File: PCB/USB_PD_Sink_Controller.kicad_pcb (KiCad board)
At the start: 2 copper layers, 43.5 x 30.8 mm, 26 parts, among them J1 USB_C_Receptacle_PowerOnly_6P, J2 JST_01x02_Socket, U1 STUSB4500QTR, U2 STL6P3LLH6, U3 STL6P3LLH6

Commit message: Added Ground plane and started LDO addition to SCH
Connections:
- A1 pad 27: unconnected-(A1-+5V-Pad27) -> Net-(A1-+5V)
- A1 pad 30: unconnected-(A1-VIN-Pad30) -> /Vbus
- J2 pad 1: Net-(D4-K) -> GND
- J2 pad 2: GND -> Net-(D4-K)
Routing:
- net GND: track 154.9 -> 72.1 mm
- net /Vbus: track 45.2 -> 78.7 mm
- net Net-(D4-K): track 18.9 -> 19.8 mm
- added copper zone on B.Cu, net GND

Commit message: Made the Arduino esp32 and added a diode to prevent reverse voltage
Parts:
- added D5: D, Diode_SMD:D_0603_1608Metric_Pad1.05x0.95mm_HandSolder, F.Cu at (350.5, 124.2)
- A1: value Arduino_Nano_v2.x -> Arduino_Nano_ESP32
- J2: footprint Connector_JST:JST_XH_B2B-XH-AM_1x02_P2.50mm_Vertical -> Connector_JST:JST_XH_B2B-XH-A_1x02_P2.50mm_Vertical
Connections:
- A1 pad 17: unconnected-(A1-3V3-Pad17) -> /VSYS
- A1 pad 27: Net-(A1-+5V) -> unconnected-(A1-VUSB/5V-Pad27)
- A1 pad 30: /Vbus -> Net-(A1-VIN)
- U1 pad 22: GND -> /VSYS
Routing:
- net /VSYS: track 0.00 -> 29.0 mm, vias 0 -> 2
- net GND: track 72.1 -> 44.9 mm, vias 1 -> 3
- net /DISCH: track 0.00 -> 24.7 mm, vias 0 -> 2
- net /Vbus: track 78.7 -> 59.1 mm, vias 4 -> 5
- net Net-(A1-VIN): track 0.00 -> 19.2 mm
- net Net-(U2-G): track 13.6 -> 14.8 mm, vias 0 -> 2
- net Net-(U1-VREG_2V7): track 1.92 -> 2.69 mm

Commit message: Updated PCB
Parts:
- removed A1: Arduino_Nano_ESP32, Module:Arduino_Nano
- removed D5: D, Diode_SMD:D_0603_1608Metric_Pad1.05x0.95mm_HandSolder
- added J3: JST_01x05_Socket, Connector_JST:JST_XH_B5B-XH-A_1x05_P2.50mm_Vertical, F.Cu at (345.5, 122.0)
- moved R7 18.1 mm to (328.9, 124.5)
- moved R6 13.3 mm to (340.5, 120.0)
- moved D4 9.13 mm to (341.5, 124.6), turned to -90 degrees
- moved R9 5.82 mm to (334.3, 122.3), turned to 0 degrees
- moved R8 5.06 mm to (338.7, 125.1)
- moved R10 4.43 mm to (340.5, 121.6), turned to 0 degrees
- moved R5 4.30 mm to (347.0, 118.2)
- moved C6 4.00 mm to (347.0, 116.8)
- moved R3 3.64 mm to (343.5, 118.2)
- moved J2 2.72 mm to (353.0, 115.0), turned to 0 degrees
- moved U2 2.51 mm to (342.4, 114.0)
- moved R4 2.50 mm to (343.5, 116.8), turned to 0 degrees
- moved U3 2.45 mm to (347.5, 114.0)
- moved R1 1.77 mm to (334.0, 118.0)
- moved R2 1.28 mm to (334.5, 119.5)
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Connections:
- C1 pad 1: /Vbus -> /VDD
- C3 pad 1: GND -> /VDD
- C3 pad 2: /VDD -> GND
- C4 pad 1: GND -> Net-(U1-VREG_2V7)
- C4 pad 2: Net-(U1-VREG_2V7) -> GND
- C5 pad 1: GND -> Net-(U1-VREG_1V2)
- C5 pad 2: Net-(U1-VREG_1V2) -> GND
- D1 pad 1: /Vbus -> /VDD
- D3 pad 2: /Vbus -> /VDD
- J1 pad A9: /Vbus -> /VDD
- J1 pad B9: /Vbus -> /VDD
- R1 pad 1: /Vbus -> /VDD
- R10 pad 1: Net-(A1-SDA/A4) -> Net-(U1-SDA)
- R4 pad 2: /VDD -> Net-(U2-S)
- R7 pad 1: /RESET -> GND
- R7 pad 2: GND -> /RESET
- R8 pad 1: Net-(A1-D3) -> /ALERT
- R8 pad 2: /ALERT -> Net-(U1-SCL)
- R9 pad 1: Net-(A1-SCL/A5) -> Net-(U1-ALERT)
- U1 pad 19: /SCL -> Net-(U1-ALERT)
- U1 pad 22: /VSYS -> /3V3
- U1 pad 7: /ALERT -> Net-(U1-SCL)
- U1 pad 8: /SDA -> Net-(U1-SDA)
- U2 pad 2: /VDD -> Net-(U2-S)
- U2 pad 3: /Vbus -> /VDD
- U3 pad 2: /VDD -> Net-(U2-S)
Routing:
- net /Vbus: track 59.1 -> 0.00 mm, vias 5 -> 0
- net /VDD: track 22.7 -> 52.0 mm, vias 2 -> 4
- net /VSYS: track 29.0 -> 0.00 mm, vias 2 -> 0
- net /RESET: track 27.9 -> 2.48 mm, vias 1 -> 0
- net Net-(D4-K): track 19.8 -> 44.7 mm
- net /3V3: track 0.00 -> 22.2 mm, vias 0 -> 1
- net Net-(A1-SCL/A5): track 22.0 -> 0.00 mm, vias 2 -> 0
- net Net-(A1-SDA/A4): track 21.9 -> 0.00 mm, vias 2 -> 0
- net Net-(A1-VIN): track 19.2 -> 0.00 mm
- net Net-(U1-SDA): track 0.00 -> 14.1 mm
- net /DISCH: track 24.7 -> 12.3 mm, vias 2 -> 0
- net Net-(U1-SCL): track 0.00 -> 11.5 mm
- net /SCL: track 9.69 -> 20.6 mm
- net GND: track 44.9 -> 36.2 mm
- net Net-(A1-D3): track 7.64 -> 0.00 mm, vias 2 -> 0
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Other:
- board size 43.5 x 30.8 mm -> 43.5 x 13.9 mm
- board text added: "3V3"
- board text added: "ALT"
- board text added: "GND"
- board text added: "SCL"
- board text added: "SDA"
- board text added: "VBUS"

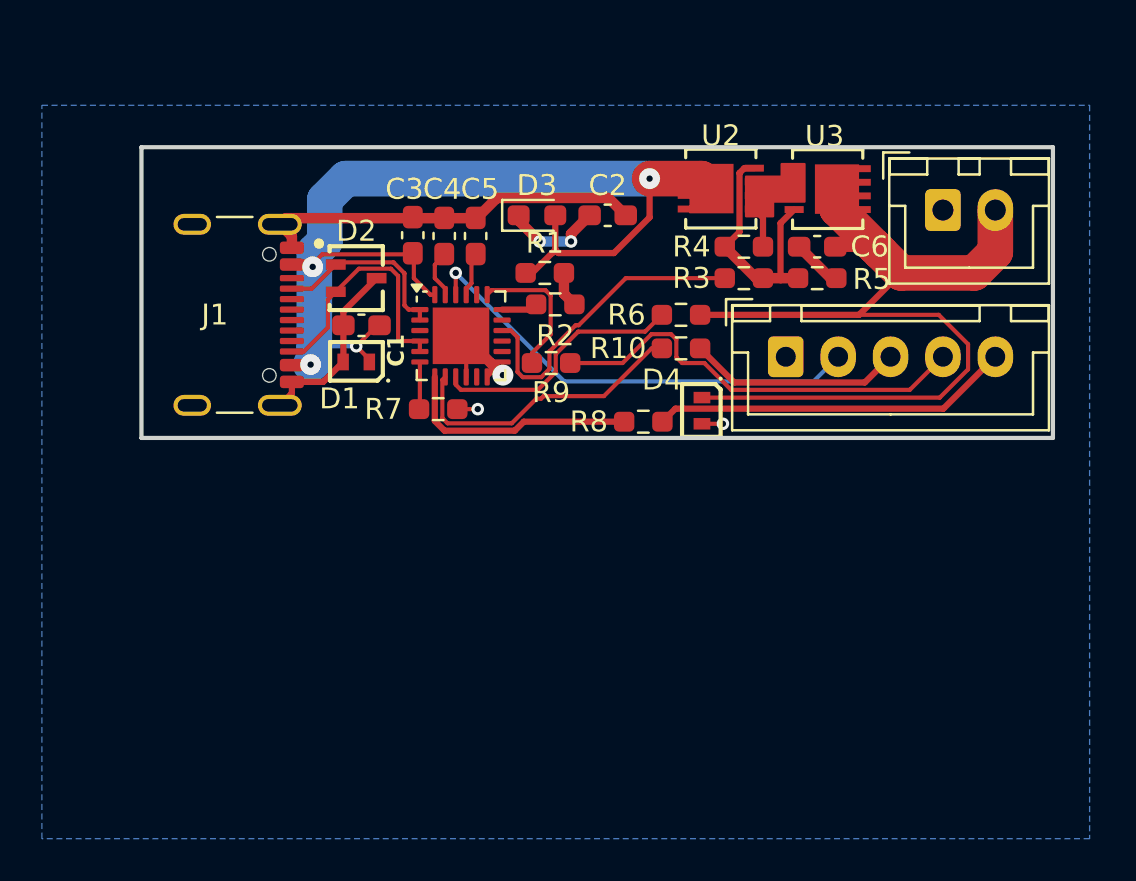
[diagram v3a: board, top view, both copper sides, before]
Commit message: Made min VBUS main and added BOM
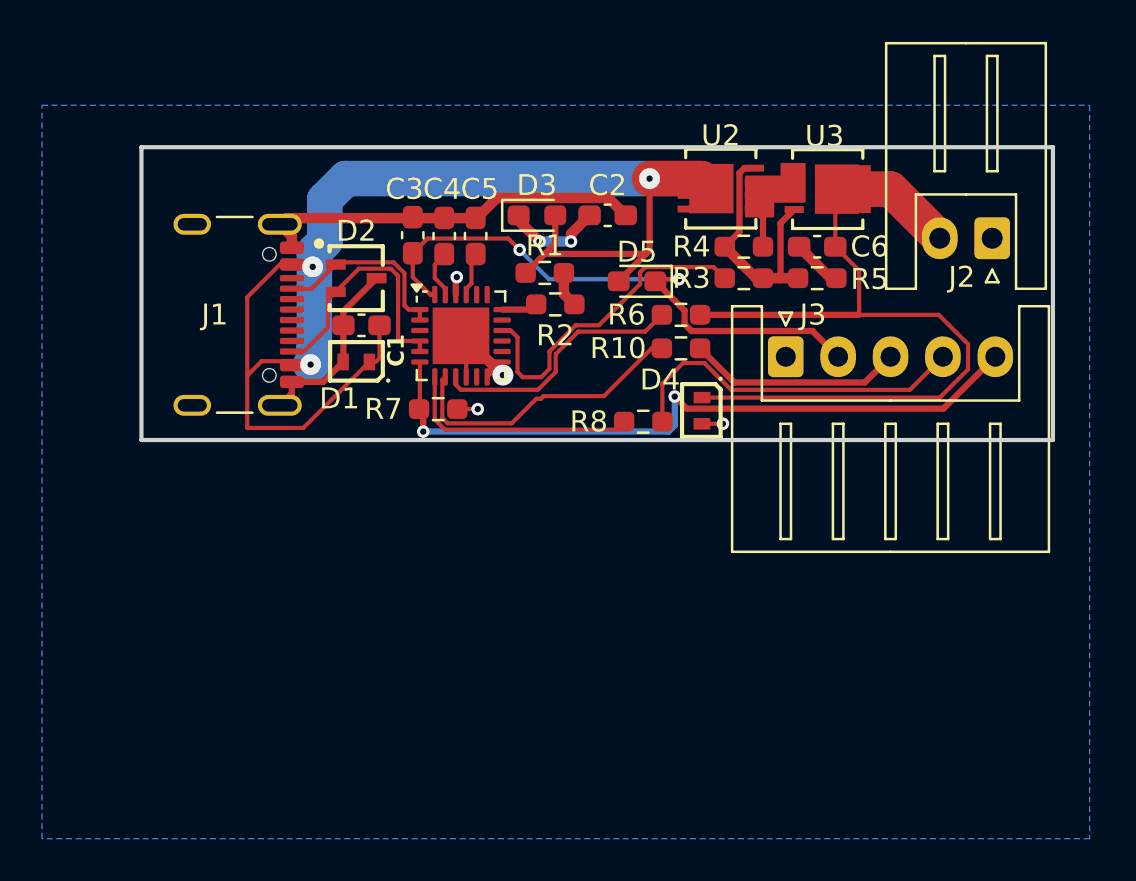
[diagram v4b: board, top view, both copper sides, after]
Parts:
- removed R9: 4.7kR, Resistor_SMD:R_0603_1608Metric_Pad0.98x0.95mm_HandSolder
- added D5: D, Diode_SMD:D_0603_1608Metric_Pad1.05x0.95mm_HandSolder, F.Cu at (338.4, 118.4)
- J2: footprint Connector_JST:JST_XH_B2B-XH-A_1x02_P2.50mm_Vertical -> Connector_JST:JST_XH_S2B-XH-A_1x02_P2.50mm_Horizontal
- J3: footprint Connector_JST:JST_XH_B5B-XH-A_1x05_P2.50mm_Vertical -> Connector_JST:JST_XH_S5B-XH-A_1x05_P2.50mm_Horizontal
- moved J2 2.71 mm to (355.4, 116.3), turned to 180 degrees
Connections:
- C1 pad 1: /VDD -> /Vbus
- D1 pad 1: /VDD -> /Vbus
- D3 pad 2: /VDD -> /Vbus
- J1 pad A9: /VDD -> /Vbus
- J1 pad B9: /VDD -> /Vbus
- J3 pad 2: /3V3 -> /VDD
- J3 pad 5: /ALERT -> /RESET
- R1 pad 1: /VDD -> /Vbus
- R8 pad 1: /ALERT -> /SCL
- U1 pad 19: Net-(U1-ALERT) -> unconnected-(U1-ALERT-Pad19)
- U1 pad 22: /3V3 -> GND
- U2 pad 3: /VDD -> /Vbus
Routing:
- net /Vbus: track 0.00 -> 63.7 mm, vias 0 -> 3
- net /RESET: track 2.48 -> 33.6 mm, vias 0 -> 2
- net /VDD: track 52.0 -> 28.1 mm, vias 4 -> 2
- net /3V3: track 22.2 -> 0.00 mm, vias 1 -> 0
- net /ALERT: track 17.2 -> 0.00 mm
- net Net-(U1-ALERT): track 6.82 -> 0.00 mm
- net Net-(D4-K): track 44.7 -> 40.2 mm
- net /SCL: track 20.6 -> 16.8 mm
- net /VBUS_EN_SNK: track 15.0 -> 15.7 mm
- net GND: track 36.2 -> 36.6 mm, vias 3 -> 4
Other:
- board size 43.5 x 13.9 mm -> 43.5 x 14 mm
- board text added: "STUSB-1-0"
- board text added: "VDD"
- board text removed: "3V3"

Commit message: cleanup on some files and PCB
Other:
- board text added: "RST"
- board text removed: "ALT"
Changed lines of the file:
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@@
 		)
 		(fp_text user "${REFERENCE}"
-			(at 5 3.45 0)
+			(at 1 5.5 0)
 			(layer "F.Fab")
 			(effects
@@
 		(layer "Edge.Cuts")
 	)
-	(gr_text "ALT"
-		(at 356.1 123.2 90)
+	(gr_text "RST"
+		(at 356.25 123.25 90)
 		(layer "B.SilkS")
 		(effects
 			(font
-				(size 1 1)
+				(size 0.8 0.8)
 				(thickness 0.1)
 			)
@@
 	)
 	(gr_text "VBUS"
-		(at 356.1 116.3 90)
+		(at 353.25 117.75 90)
 		(layer "B.SilkS")
 		(effects
 			(font
-				(size 1 1)
+				(size 0.6 0.6)
 				(thickness 0.1)
 			)
@@
 	)
 	(gr_text "VDD"
-		(at 348.5 123 90)
+		(at 348.5 123.5 90)
 		(layer "B.SilkS")
 		(effects
 			(font
-				(size 1 1)
+				(size 0.8 0.8)
 				(thickness 0.1)
 			)
@@
 	)
 	(gr_text "GND"
-		(at 346 122.9 90)
+		(at 346 123.25 90)
 		(layer "B.SilkS")
 		(effects
 			(font
-				(size 1 1)
+				(size 0.8 0.8)
 				(thickness 0.1)
 			)
@@
 	)
 	(gr_text "GND"
-		(at 353.6 116.3 90)
+		(at 355.75 117.75 90)
 		(layer "B.SilkS")
 		(effects
 			(font
-				(size 1 1)
+				(size 0.6 0.6)
 				(thickness 0.1)
 			)
@@
 	)
 	(gr_text "SDA"
-		(at 351.1 122.9 90)
+		(at 351 123.25 90)
 		(layer "B.SilkS")
 		(effects
 			(font
-				(size 1 1)
+				(size 0.8 0.8)
 				(thickness 0.1)
 			)
@@
 	)
 	(gr_text "SCL"
-		(at 353.6 122.9 90)
+		(at 353.75 123.25 90)
 		(layer "B.SilkS")
 		(effects
 			(font
-				(size 1 1)
+				(size 0.8 0.8)
 				(thickness 0.1)
 			)
